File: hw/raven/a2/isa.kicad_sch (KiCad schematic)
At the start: 25 parts, among them J501 ISA16, J502 ISA16, J503 ISA16, J504 ISA16, U501 ATF22V10C-10PU, X501 14.31818Mhz (5V)

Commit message: misc a2 work
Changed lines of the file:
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@@
 		)
 	)
-	(text_box "TODO:\nAbility to choose\nSMEMx vs MEMx\n\nThey are both the same\nat the moment."
+	(text_box "IGNORE. POINTLESS.\nNo ISA card cares.\n\n(but keeping for info)\nAbility to choose\nSMEMx vs MEMx\nThey are both the same\nat the moment."
 		(exclude_from_sim no)
 		(at 115.57 66.675 0)
@@
 		(stroke
 			(width 0)
-			(type default)
-		)
-		(fill
-			(type color)
-			(color 255 230 63 0.53)
-		)
-		(effects
-			(font
-				(size 1.27 1.27)
-				(color 0 0 0 1)
-			)
-			(justify left top)
-		)
-	)
-	(text_box "FIXME:\n\nISA interrupts should be pulled high.\nCards will pull them low for x cycles and release.\n\nPC detects it on the low->high transition.\n"
-		(exclude_from_sim no)
-		(at 147.955 374.015 0)
-		(size 46.355 20.32)
-		(margins 0.9525 0.9525 0.9525 0.9525)
-		(stroke
-			(width 0)
 			(type solid)
 		)
 		(fill
-			(type color)
-			(color 255 230 63 0.53)
+			(type none)
 		)
 		(effects
 			(font
 				(size 1.27 1.27)
-				(color 0 0 0 1)
+				(color 194 194 194 1)
 			)
 			(justify left top)
@@
 	(wire
 		(pts
+			(xy 143.51 285.115) (xy 155.575 285.115)
+		)
+		(stroke
+			(width 0)
+			(type default)
+		)
+	)
+	(wire
+		(pts
 			(xy 280.67 269.875) (xy 292.735 269.875)
 		)
@@
 	(wire
 		(pts
-			(xy 156.845 282.575) (xy 143.51 282.575)
-		)
-		(stroke
-			(width 0)
-			(type default)
-		)
-	)
-	(wire
-		(pts
 			(xy 498.475 335.915) (xy 510.54 335.915)
 		)
@@
 	(wire
 		(pts
+			(xy 143.51 290.195) (xy 155.575 290.195)
+		)
+		(stroke
+			(width 0)
+			(type default)
+		)
+	)
+	(wire
+		(pts
 			(xy 259.715 207.01) (xy 259.715 205.105)
 		)
@@
 	(wire
 		(pts
-			(xy 156.845 292.735) (xy 143.51 292.735)
-		)
-		(stroke
-			(width 0)
-			(type default)
-		)
-	)
-	(wire
-		(pts
 			(xy 389.89 262.255) (xy 401.955 262.255)
 		)
@@
 	(wire
 		(pts
+			(xy 143.51 287.655) (xy 155.575 287.655)
+		)
+		(stroke
+			(width 0)
+			(type default)
+		)
+	)
+	(wire
+		(pts
 			(xy 498.475 297.815) (xy 510.54 297.815)
 		)
@@
 	(wire
 		(pts
-			(xy 156.845 287.655) (xy 143.51 287.655)
-		)
-		(stroke
-			(width 0)
-			(type default)
-		)
-	)
-	(wire
-		(pts
 			(xy 222.885 302.895) (xy 234.95 302.895)
 		)
@@
 		)
 	)
-	(wire
-		(pts
-			(xy 156.845 277.495) (xy 143.51 277.495)
-		)
-		(stroke
-			(width 0)
-			(type default)
-		)
-	)
 	(bus
 		(pts
@@
 	(wire
 		(pts
+			(xy 143.51 277.495) (xy 155.575 277.495)
+		)
+		(stroke
+			(width 0)
+			(type default)
+		)
+	)
+	(wire
+		(pts
 			(xy 42.545 244.475) (xy 50.165 244.475)
 		)
@@
 	(wire
 		(pts
+			(xy 143.51 282.575) (xy 155.575 282.575)
+		)
+		(stroke
+			(width 0)
+			(type default)
+		)
+	)
+	(wire
+		(pts
 			(xy 212.09 280.035) (xy 234.95 280.035)
 		)
@@
 	(wire
 		(pts
+			(xy 143.51 280.035) (xy 155.575 280.035)
+		)
+		(stroke
+			(width 0)
+			(type default)
+		)
+	)
+	(wire
+		(pts
 			(xy 222.885 332.74) (xy 234.95 332.74)
 		)
@@
 		)
 	)
-	(wire
-		(pts
-			(xy 156.845 290.195) (xy 143.51 290.195)
-		)
-		(stroke
-			(width 0)
-			(type default)
-		)
-	)
 	(bus
 		(pts
@@
 	(wire
 		(pts
-			(xy 156.845 280.035) (xy 143.51 280.035)
-		)
-		(stroke
-			(width 0)
-			(type default)
-		)
-	)
-	(wire
-		(pts
-			(xy 156.845 285.115) (xy 143.51 285.115)
-		)
-		(stroke
-			(width 0)
-			(type default)
-		)
-	)
-	(wire
-		(pts
 			(xy 41.91 252.095) (xy 49.53 252.095)
 		)
@@
 	(wire
 		(pts
-			(xy 143.51 264.795) (xy 156.845 264.795)
+			(xy 143.51 264.795) (xy 155.575 264.795)
 		)
 		(stroke
@@
 		)
 		(stroke
+			(width 0)
+			(type default)
+		)
+	)
+	(wire
+		(pts
+			(xy 143.51 292.735) (xy 155.575 292.735)
+		)
+		(stroke

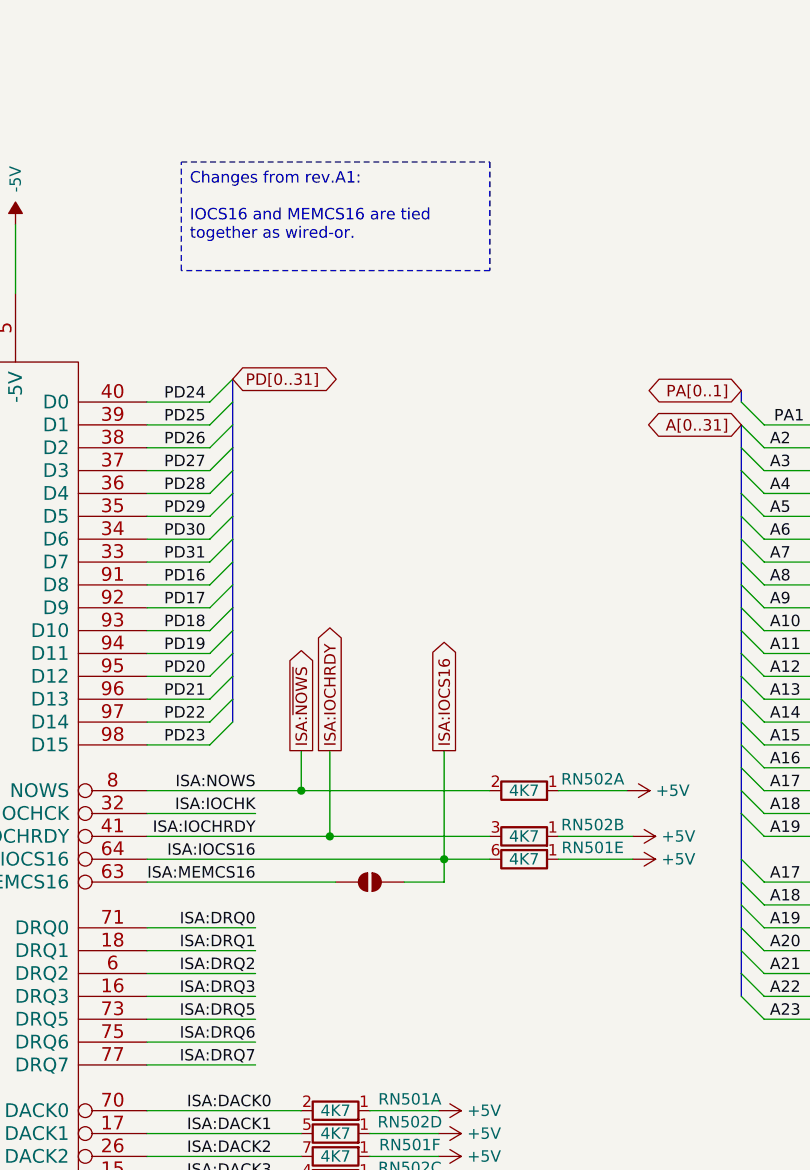
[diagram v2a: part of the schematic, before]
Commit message: A2: schema + routing complete. ERC + DRC complete.
Let sit for a while, revisit and sanity check with fresh eyes before gerber.
Todo: double check BOM export and fix missing infos if any.
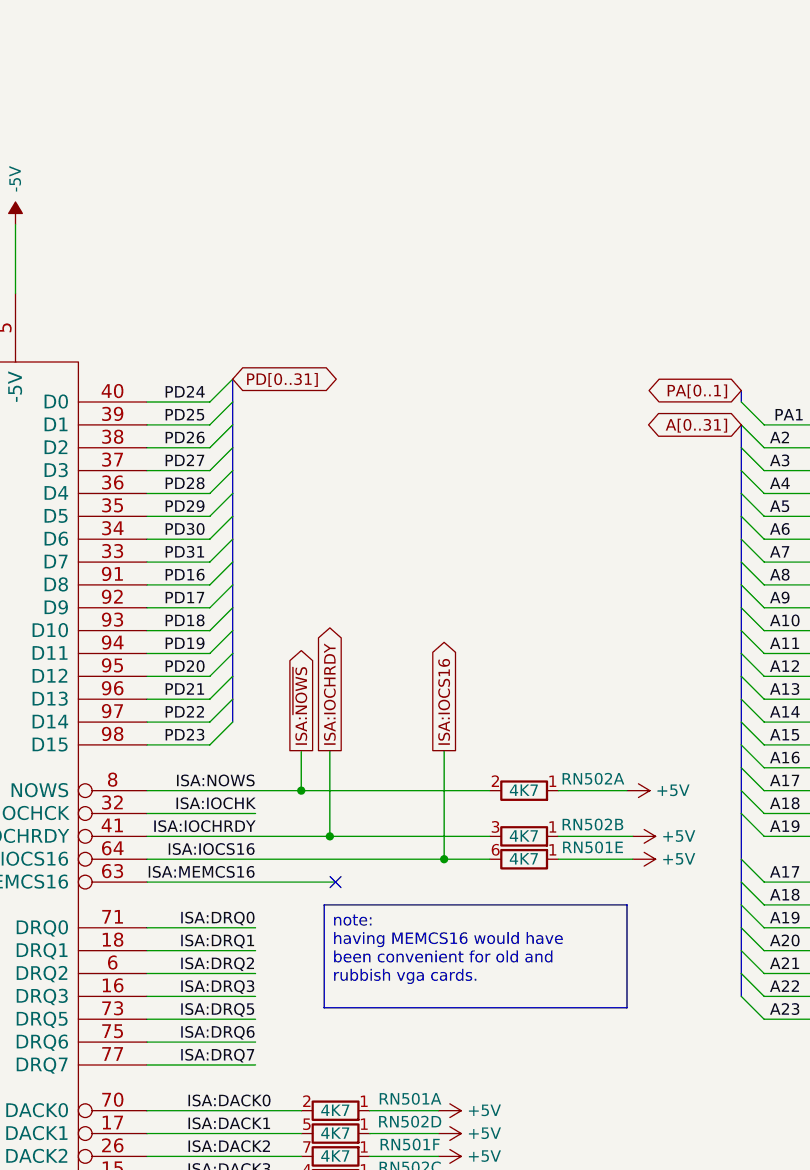
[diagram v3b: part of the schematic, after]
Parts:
- removed JP501: SolderJumper_2_Bridged, Jumper:SolderJumper-2_P1.3mm_Open_RoundedPad1.0x1.5mm, symbol Jumper:SolderJumper_2_Open
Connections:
- no-connect marks 6 -> 7
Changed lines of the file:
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@@
 		)
 	)
-	(text_box "IGNORE. POINTLESS.\nNo ISA card cares.\n\n(but keeping for info)\nAbility to choose\nSMEMx vs MEMx\nThey are both the same\nat the moment."
+	(text_box "note:\nhaving MEMCS16 would have\nbeen convenient for old and\nrubbish vga cards."
 		(exclude_from_sim no)
-		(at 115.57 66.675 0)
-		(size 31.115 17.78)
+		(at 163.195 274.955 0)
+		(size 33.655 11.43)
 		(margins 0.9525 0.9525 0.9525 0.9525)
 		(stroke
@@
 		)
 	)
-	(text_box "Changes from rev.A1:\n\nIOCS16 and MEMCS16 are tied\ntogether as wired-or.\n"
+	(text_box "IGNORE. POINTLESS.\nNo ISA card cares.\n\n(but keeping for info)\nAbility to choose\nSMEMx vs MEMx\nThey are both the same\nat the moment."
 		(exclude_from_sim no)
-		(at 147.32 192.405 0)
-		(size 34.29 12.065)
+		(at 115.57 66.675 0)
+		(size 31.115 17.78)
 		(margins 0.9525 0.9525 0.9525 0.9525)
 		(stroke
 			(width 0)
-			(type dot)
+			(type solid)
 		)
 		(fill
@@
 			(font
 				(size 1.27 1.27)
+				(color 194 194 194 1)
 			)
 			(justify left top)
@@
 		(at 33.02 244.475)
 	)
+	(no_connect
+		(at 164.465 272.415)
+	)
 	(bus_entry
 		(at 72.39 257.175)
@@
 	(wire
 		(pts
-			(xy 176.53 272.415) (xy 176.53 269.875)
-		)
-		(stroke
-			(width 0)
-			(type default)
-		)
-	)
-	(wire
-		(pts
 			(xy 389.89 297.815) (xy 401.955 297.815)
 		)
@@
 	(wire
 		(pts
-			(xy 172.085 272.415) (xy 176.53 272.415)
-		)
-		(stroke
-			(width 0)
-			(type default)
-		)
-	)
-	(wire
-		(pts
 			(xy 74.93 231.775) (xy 97.79 231.775)
 		)
@@
 		)
 	)
+	(wire
+		(pts
+			(xy 143.51 272.415) (xy 164.465 272.415)
+		)
+		(stroke
+			(width 0)
+			(type default)
+		)
+	)
 	(bus
 		(pts
@@
 	(wire
 		(pts
-			(xy 143.51 272.415) (xy 164.465 272.415)
-		)
-		(stroke
-			(width 0)
-			(type default)
-		)
-	)
-	(wire
-		(pts
 			(xy 429.895 264.795) (xy 452.755 264.795)
 		)
@@
 			)
 		)
-		(property "Description" ""
+		(property "Description" "Crystal Clock Oscillator, DIP8-style metal package"
 			(at 33.02 332.74 0)
 			(effects
@@
 					(size 1.27 1.27)
 				)
+				(hide yes)
 			)
 		)
@@
 					(unit 1)
 				)
-			)
-		)
-	)
-	(symbol
-		(lib_id "Jumper:SolderJumper_2_Open")
-		(at 168.275 272.415 0)
-		(unit 1)
-		(exclude_from_sim yes)
-		(in_bom no)
-		(on_board yes)
-		(dnp no)
-		(fields_autoplaced yes)
-		(property "Reference" "JP501"
-			(at 168.275 266.065 0)
-			(effects
-				(font
-					(size 1.27 1.27)
-				)
-				(hide yes)
-			)
-		)
-		(property "Value" "SolderJumper_2_Bridged"
-			(at 168.275 268.605 0)
-			(effects
-				(font
-					(size 1.27 1.27)
-				)
-				(hide yes)
-			)
-		)
-		(property "Footprint" "Jumper:SolderJumper-2_P1.3mm_Open_RoundedPad1.0x1.5mm"
-			(at 168.275 272.415 0)
-			(effects
-				(font
-					(size 1.27 1.27)
-				)
-				(hide yes)
-			)
-		)
-		(property "Datasheet" "~"
-			(at 168.275 272.415 0)
-			(effects
-				(font
-					(size 1.27 1.27)
-				)
-				(hide yes)
-			)
-		)
-		(property "Description" "Solder Jumper, 2-pole, open"
-			(at 168.275 272.415 0)
-			(effects
-				(font
-					(size 1.27 1.27)
-				)
-				(hide yes)
-			)
-		)
-		(pin "1"
-		)
-		(pin "2"
-		)
-		(instances
-			(project ""
-				(path "/af55e73e-5814-45b4-ac5c-0bab62c0b1c7/eec73fb6-6eba-45b9-9adf-00542ef5d3d8"
-					(reference "JP501")
-					(unit 1)
-				)

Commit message: A2: cosmetics and bom preparations
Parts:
- C502, C503, C504, C505, C506, C507, C508, C509, C510, C511, C512, C513: footprint Capacitor_THT:CP_Radial_D5.0mm_P2.50mm -> Capacitor_THT:CP_Radial_D6.3mm_P2.50mm; Manufacturer_Part_Number EEU-EB1H100SH -> ECE-A1HKS100I
- U501: value ATF22V10C-10PU -> ATF22V10
